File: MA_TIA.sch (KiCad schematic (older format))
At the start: 43 parts, among them J1 pwr_input_5V, J2 Signal_Out, J3 Photodiode_conn, J4 digital_pwr, J5 analog_supply, J6 digital_interface, U1 TMA0505D, U2 ADA4350, U3 TPS79301-EP, U4 MIC5270

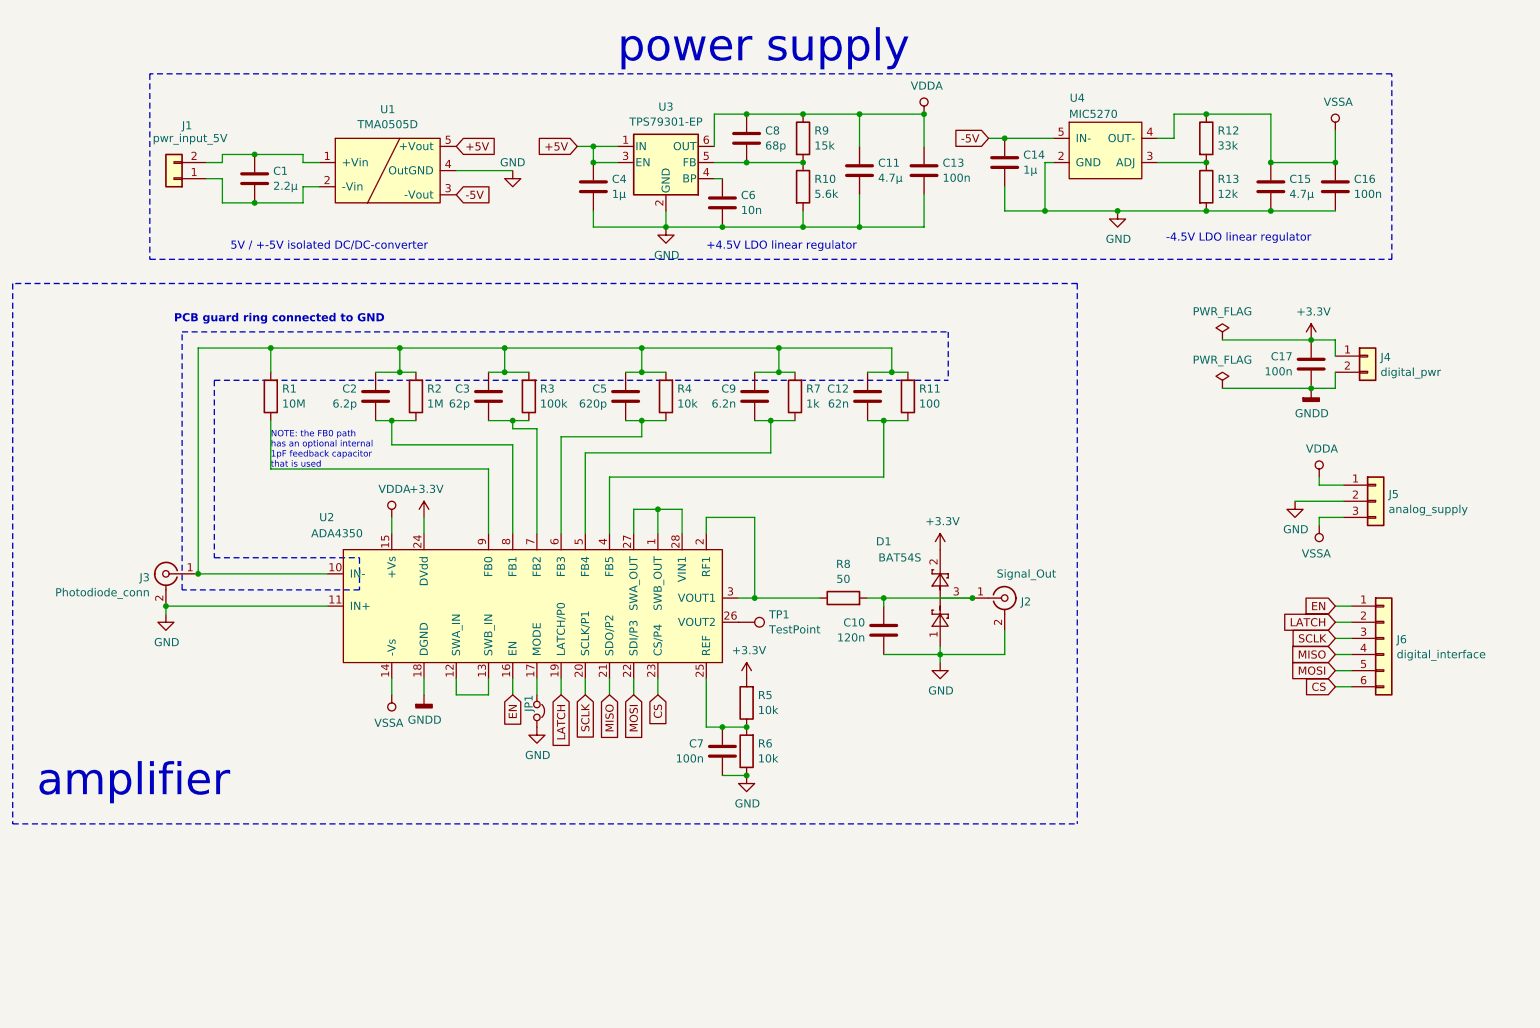
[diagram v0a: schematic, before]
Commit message: fix: removed separate digital ground
fix: removed separate digital ground (GNDD) and connected it to GND
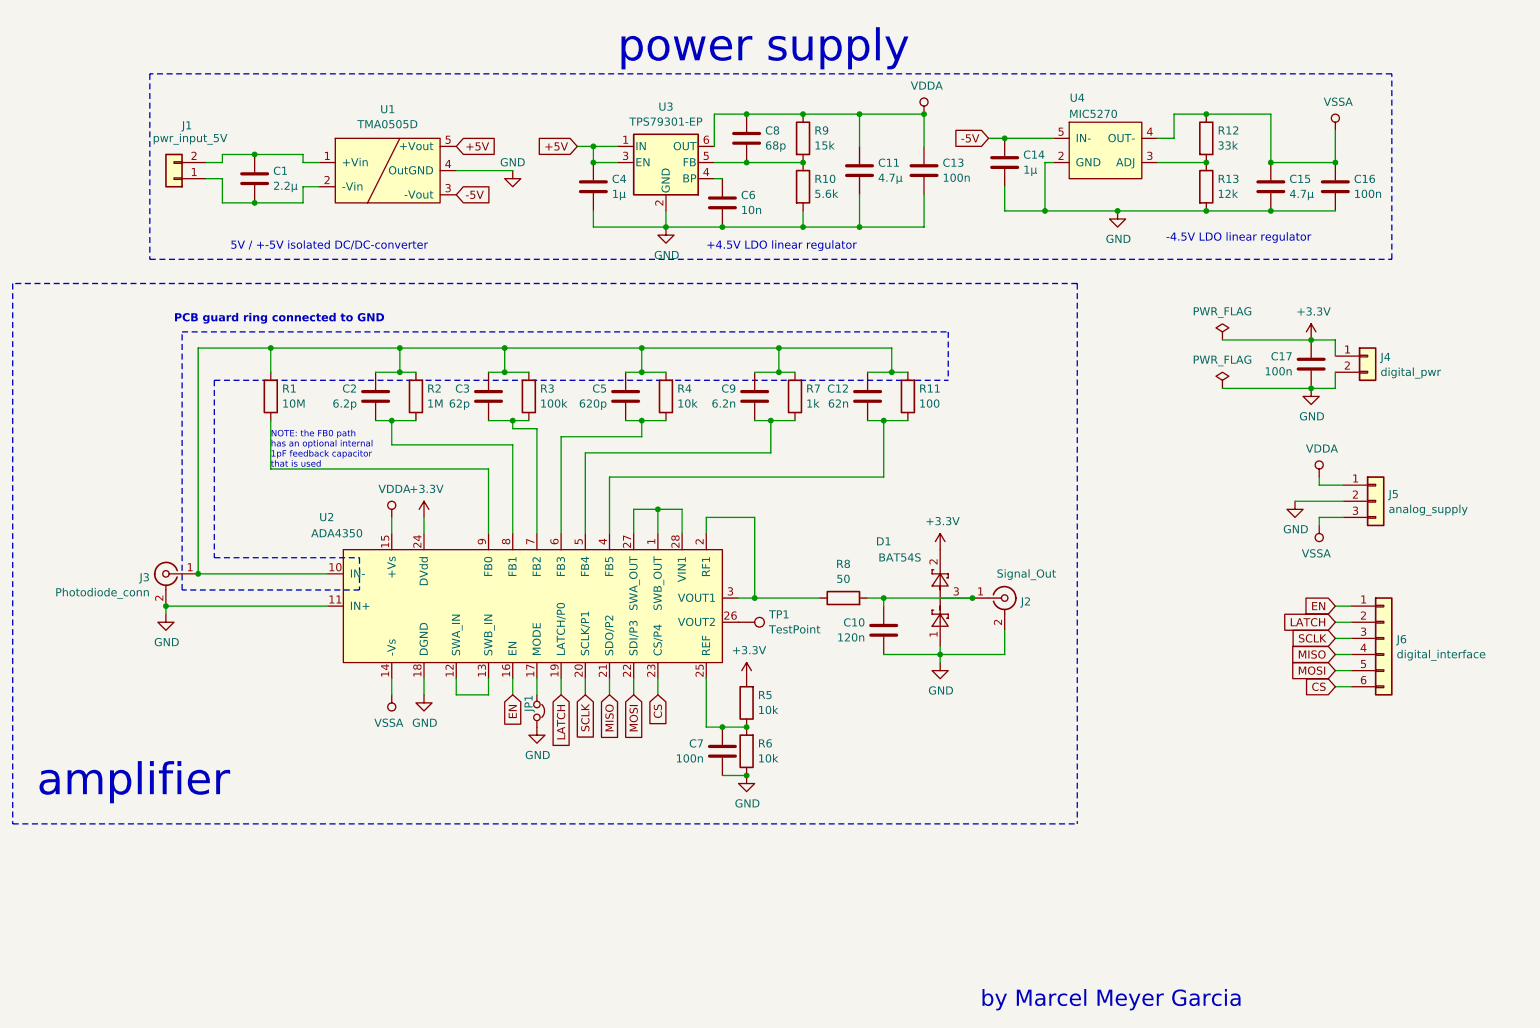
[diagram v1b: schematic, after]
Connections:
- net GNDD is gone; now on net GND: C17.1, J4.2 (Pin_2), U2.18 (DGND)
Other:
- note added: "by Marcel Meyer Garcia"
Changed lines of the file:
@@
 Connection ~ 6850 1450
-$Comp
-L power:GNDD #PWR01
-U 1 1 5DC88786
-P 3750 5050
-F 0 "#PWR01" H 3750 4800 50  0001 C CNN
-F 1 "GNDD" H 3754 4894 50  0000 C CNN
-F 2 "" H 3750 5050 50  0001 C CNN
-F 3 "" H 3750 5050 50  0001 C CNN
-	1    3750 5050
-	1    0    0    -1
-$EndComp
 $Comp
 L Connector_Generic:Conn_01x02 J4
@@
 F 3 "~" H 9600 2950 50  0001 C CNN
 	1    9600 2950
-	1    0    0    -1
-$EndComp
-$Comp
-L power:GNDD #PWR04
-U 1 1 5DC88BDA
-P 9250 3150
-F 0 "#PWR04" H 9250 2900 50  0001 C CNN
-F 1 "GNDD" H 9254 2994 50  0000 C CNN
-F 2 "" H 9250 3150 50  0001 C CNN
-F 3 "" H 9250 3150 50  0001 C CNN
-	1    9250 3150
 	1    0    0    -1
 $EndComp
@@
 	2150 4500 3150 4500
 Connection ~ 2150 4500
+Text Notes 7200 7000 0    100  ~ 0
+by Marcel Meyer Garcia
+$Comp
+L power:GND #PWR?
+U 1 1 5E1BE9AA
+P 9250 3150
+F 0 "#PWR?" H 9250 2900 50  0001 C CNN
+F 1 "GND" H 9255 2975 50  0000 C CNN
+F 2 "" H 9250 3150 50  0001 C CNN
+F 3 "" H 9250 3150 50  0001 C CNN
+	1    9250 3150
+	1    0    0    -1
+$EndComp
+$Comp
+L power:GND #PWR?
+U 1 1 5E1BEA0B
+P 3750 5050
+F 0 "#PWR?" H 3750 4800 50  0001 C CNN
+F 1 "GND" H 3755 4875 50  0000 C CNN
+F 2 "" H 3750 5050 50  0001 C CNN
+F 3 "" H 3750 5050 50  0001 C CNN
+	1    3750 5050
+	1    0    0    -1
+$EndComp
 $EndSCHEMATC
